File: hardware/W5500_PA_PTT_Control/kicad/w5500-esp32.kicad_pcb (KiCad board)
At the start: 4 copper layers, 72 x 115 mm, 30 parts, among them J1 ESP32_DevKitC_Socket_40P_25.4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, J2 DC_IN_13V8, J5 Power, J6 PTT_ON, J7 LED_PWR, J8 LED_12V, Q1 2SC1815, Q3 2SC1815, Q5 2SJ334, U1 TA48033S, U2 L7805

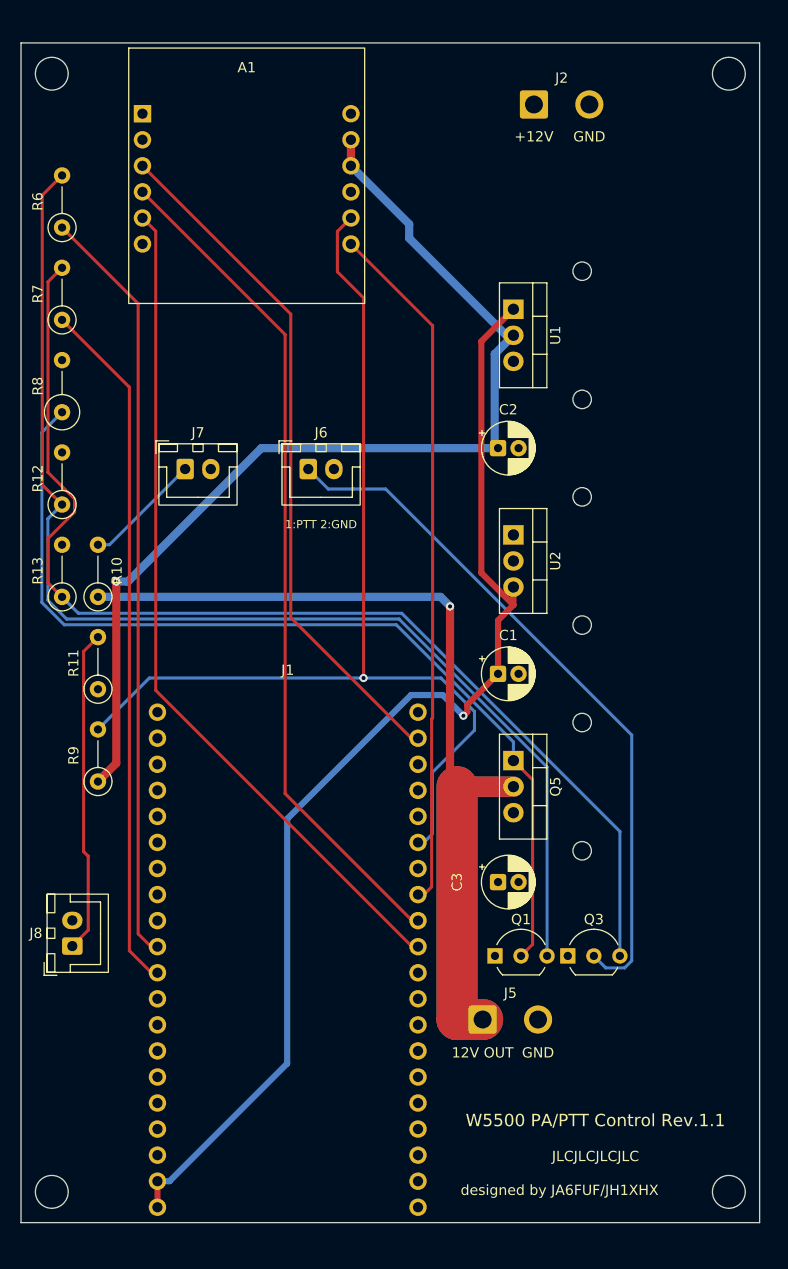
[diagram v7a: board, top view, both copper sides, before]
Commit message: W5500制御基板 Rev.1.2: 3.3VレギュレータU1をLM2940T-3.3に変更
- U1をTA48033SからLM2940T-3.3(TO-220、1=IN・2=GND・3=OUT)に変更。足の並びが違うため
  U1の2番をGND、3番を+3V3_Aにつなぎ替え、裏面の+3V3_Aの配線を引き直してベタを再充填
- C1をLM2940のデータシートどおり0.47µFに変更(C2の33µFは22µF以上・ESR 0.1〜1Ωの条件を満たす)
- U1のシンボルをproject_symbolsに追加。DRC違反0・未接続0
- シルクの版数をRev.1.2、仕様書をRev.2.8にし、版数の対応表・接続一覧を更新
- ガーバー・ドリル・ZIP・BOM・README、回路図PDF/SVG、実装図PDF、基板レイアウト画像、3D上面画像を更新

Co-Authored-By: Claude Opus 5.5 <noreply@anthropic.com>
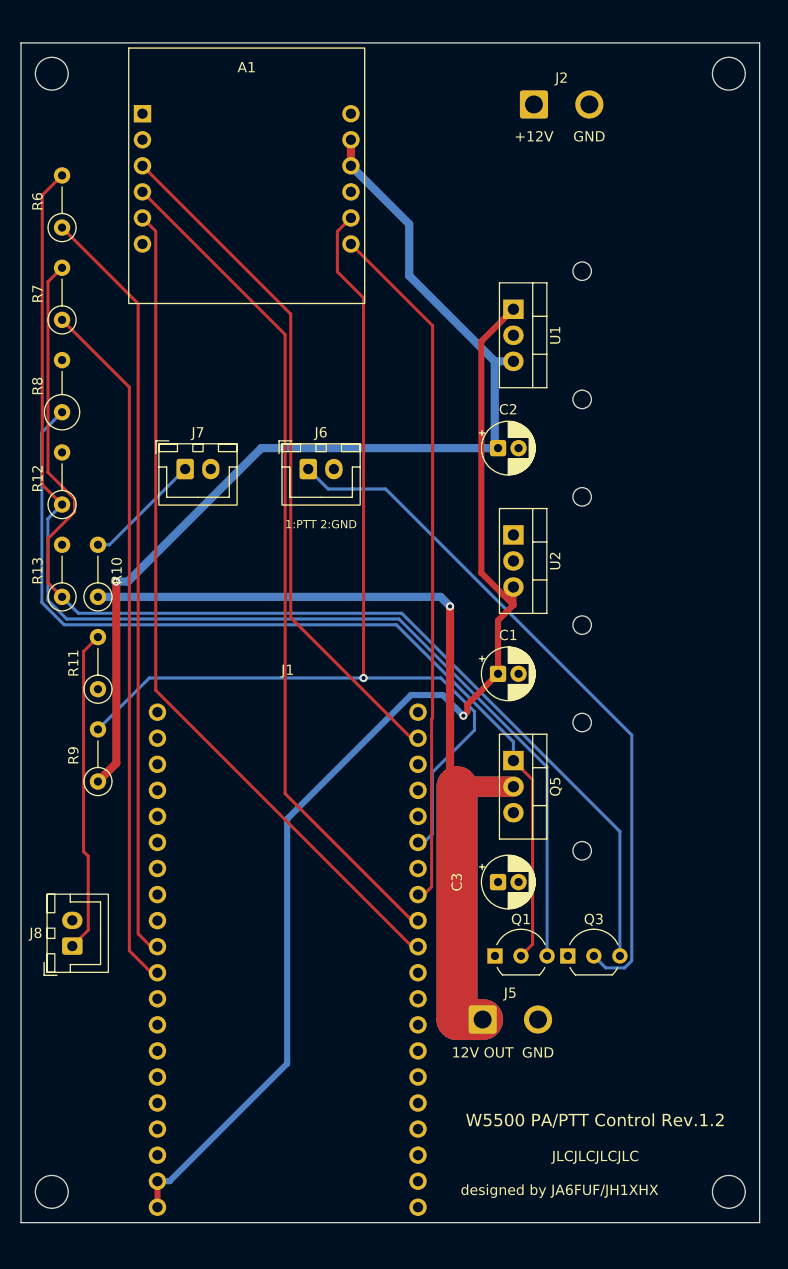
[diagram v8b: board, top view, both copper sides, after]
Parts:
- C1: value 0.33uF -> 0.47uF
- U1: value TA48033S -> LM2940T-3.3
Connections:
- U1 pad 2: /+3V3_A -> GND
- U1 pad 3: GND -> /+3V3_A
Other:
- board text added: "W5500 PA/PTT Control Rev.1.2"
- board text removed: "W5500 PA/PTT Control Rev.1.1"
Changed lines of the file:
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@@
 			)
 		)
-		(property "Description" "U1 output capacitor, electrolytic 33uF 10V or higher (TA48033S datasheet standard circuit: COUT=33uF; required for LDO stability)"
+		(property "Description" "U1 output capacitor, electrolytic 33uF 10V or higher (LM2940 datasheet: COUT>=22uF, ESR 0.1-1 ohm; required for LDO stability)"
 			(at 0 0 0)
 			(layer "F.Fab")
@@
 			)
 		)
-		(property "Value" "TA48033S"
+		(property "Value" "LM2940T-3.3"
 			(at 2.54 2.2 270)
 			(layer "F.Fab")
@@
 			)
 		)
-		(property "Datasheet" "https://akizukidenshi.com/catalog/g/g100534/"
+		(property "Datasheet" "https://www.ti.com/lit/ds/symlink/lm2940-n.pdf"
 			(at 0 0 270)
 			(layer "F.Fab")
@@
 			)
 		)
-		(property "Description" "Low dropout 3-terminal positive regulator, 3.3V 1A. IN=+12V(13.8V), OUT=+3V3_A (W5500 only). Pinout 1=IN 2=OUT 3=GND. Heatsink required (~2.1W dissipation)."
+		(property "Description" "Low dropout 3-terminal positive regulator, 3.3V 1A. IN=+5V (U2 output), OUT=+3V3_A (W5500 only). Pinout 1=IN 2=GND 3=OUT. Heatsink attached."
 			(at 0 0 270)
 			(layer "F.Fab")
@@
 			(layers "*.Cu" "*.Mask")
 			(remove_unused_layers no)
-			(net "/+3V3_A")
-			(pinfunction "OUT_2")
-			(pintype "power_out")
+			(net "GND")
+			(pinfunction "GND")
+			(pintype "power_in")
 		)
 		(pad "3" thru_hole oval
@@
 			(layers "*.Cu" "*.Mask")
 			(remove_unused_layers no)
-			(net "GND")
-			(pinfunction "GND_3")
-			(pintype "power_in")
+			(net "/+3V3_A")
+			(pinfunction "OUT")
+			(pintype "power_out")
 		)
 		(embedded_fonts no)
@@
 			)
 		)
-		(property "Value" "0.33uF"
+		(property "Value" "0.47uF"
 			(at 1 3.75 0)
 			(layer "F.Fab")
@@
 			)
 		)
-		(property "Description" "U2 output / U1 input capacitor (TA48033S datasheet: CIN=0.33uF), 16V or higher"
+		(property "Description" "U2 output / U1 input capacitor (LM2940 datasheet: CIN=0.47uF), 16V or higher"
 			(at 0 0 0)
 			(layer "F.Fab")
@@
 		)
 	)
-	(gr_text "W5500 PA/PTT Control Rev.1.1"
+	(gr_text "W5500 PA/PTT Control Rev.1.2"
 		(at 120 151.5 0)
 		(layer "F.SilkS")
@@
 	)
 	(segment
-		(start 111.6501 75.3099)
-		(end 101.8392 65.499)
+		(start 101.84 69.16)
+		(end 101.84 64.12)
 		(width 0.8)
 		(layer "B.Cu")
@@
 	)
 	(segment
-		(start 112 74.96)
-		(end 111.6501 75.3099)
+		(start 112 77.5)
+		(end 110.18 77.5)
 		(width 0.8)
 		(layer "B.Cu")
@@
 	)
 	(segment
-		(start 110.1759 85.6359)
-		(end 110.5 85.96)
+		(start 110.18 77.5)
+		(end 101.84 69.16)
 		(width 0.8)
 		(layer "B.Cu")
@@
 	)
 	(segment
-		(start 110.1759 76.7841)
-		(end 110.1759 85.6359)
+		(start 110.18 77.5)
+		(end 110.18 85.64)
 		(width 0.8)
 		(layer "B.Cu")
@@
 	)
 	(segment
-		(start 74.422 98.9675)
-		(end 87.4295 85.96)
+		(start 110.1759 85.6359)
+		(end 110.5 85.96)
 		(width 0.8)
 		(layer "B.Cu")
@@
 	)
 	(segment
-		(start 111.6501 75.3099)
-		(end 110.1759 76.7841)
+		(start 74.422 98.9675)
+		(end 87.4295 85.96)
 		(width 0.8)
 		(layer "B.Cu")
@@
 		(width 0.8)
 		(layer "B.Cu")
-		(net "/+3V3_A")
-	)
-	(segment
-		(start 101.8392 65.499)
-		(end 101.8392 64.1192)
-		(width 0.8)
-		(layer "B.Cu")
